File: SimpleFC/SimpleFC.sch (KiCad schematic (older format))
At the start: 0 parts

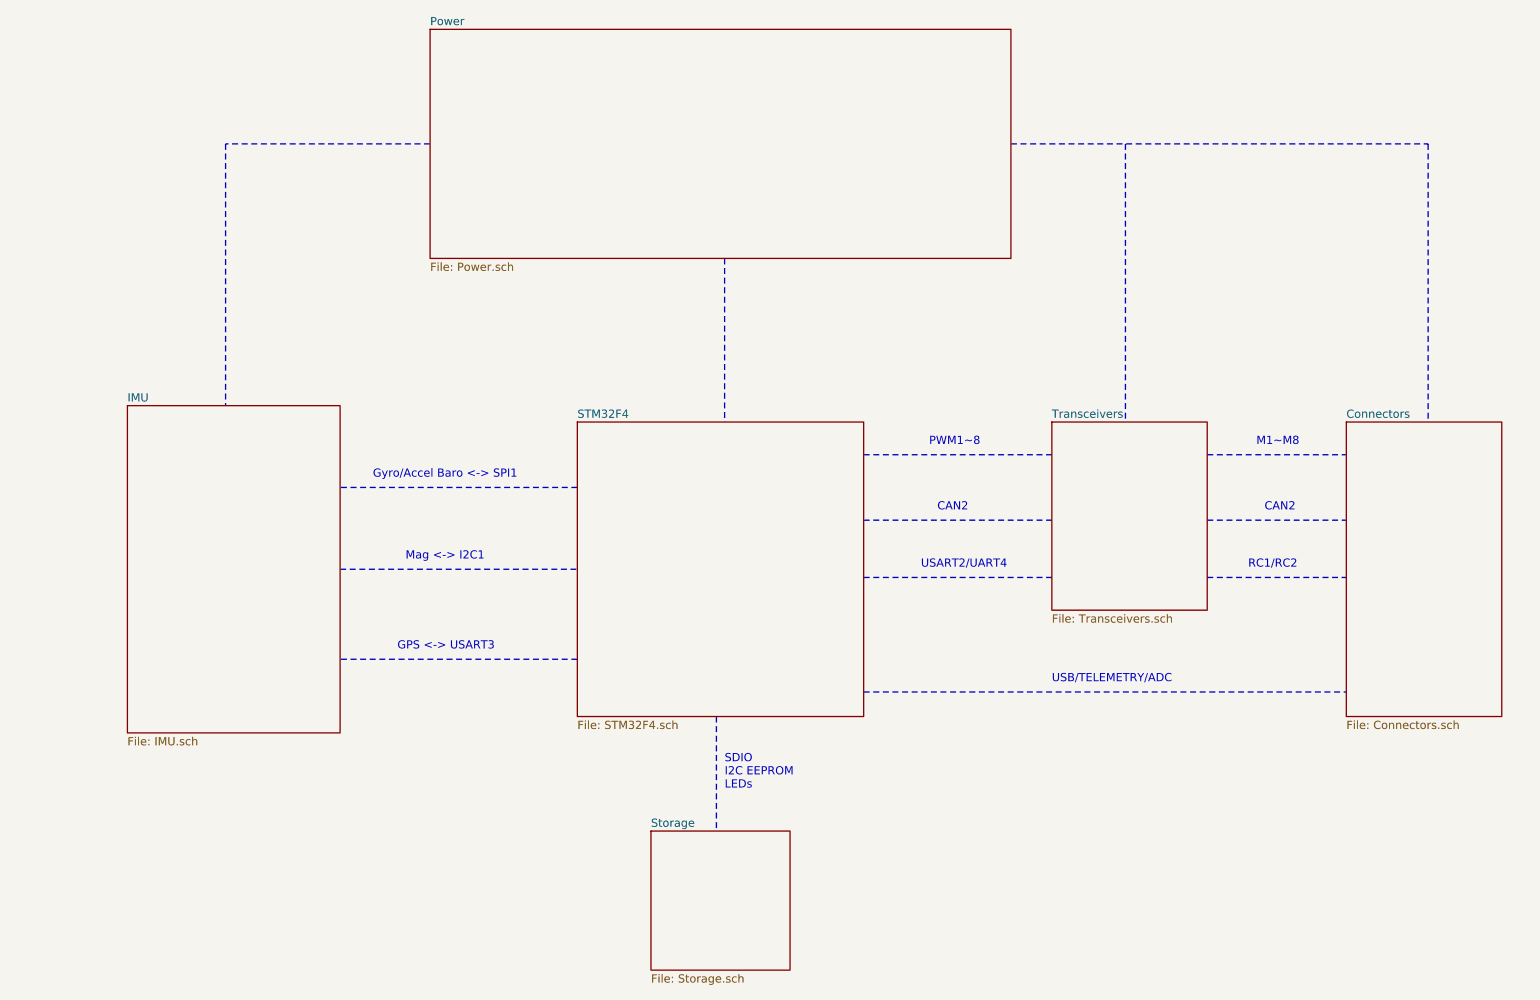
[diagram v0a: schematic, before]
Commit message: Refactor SimpleFC schematics with latest KiCAD libraries.
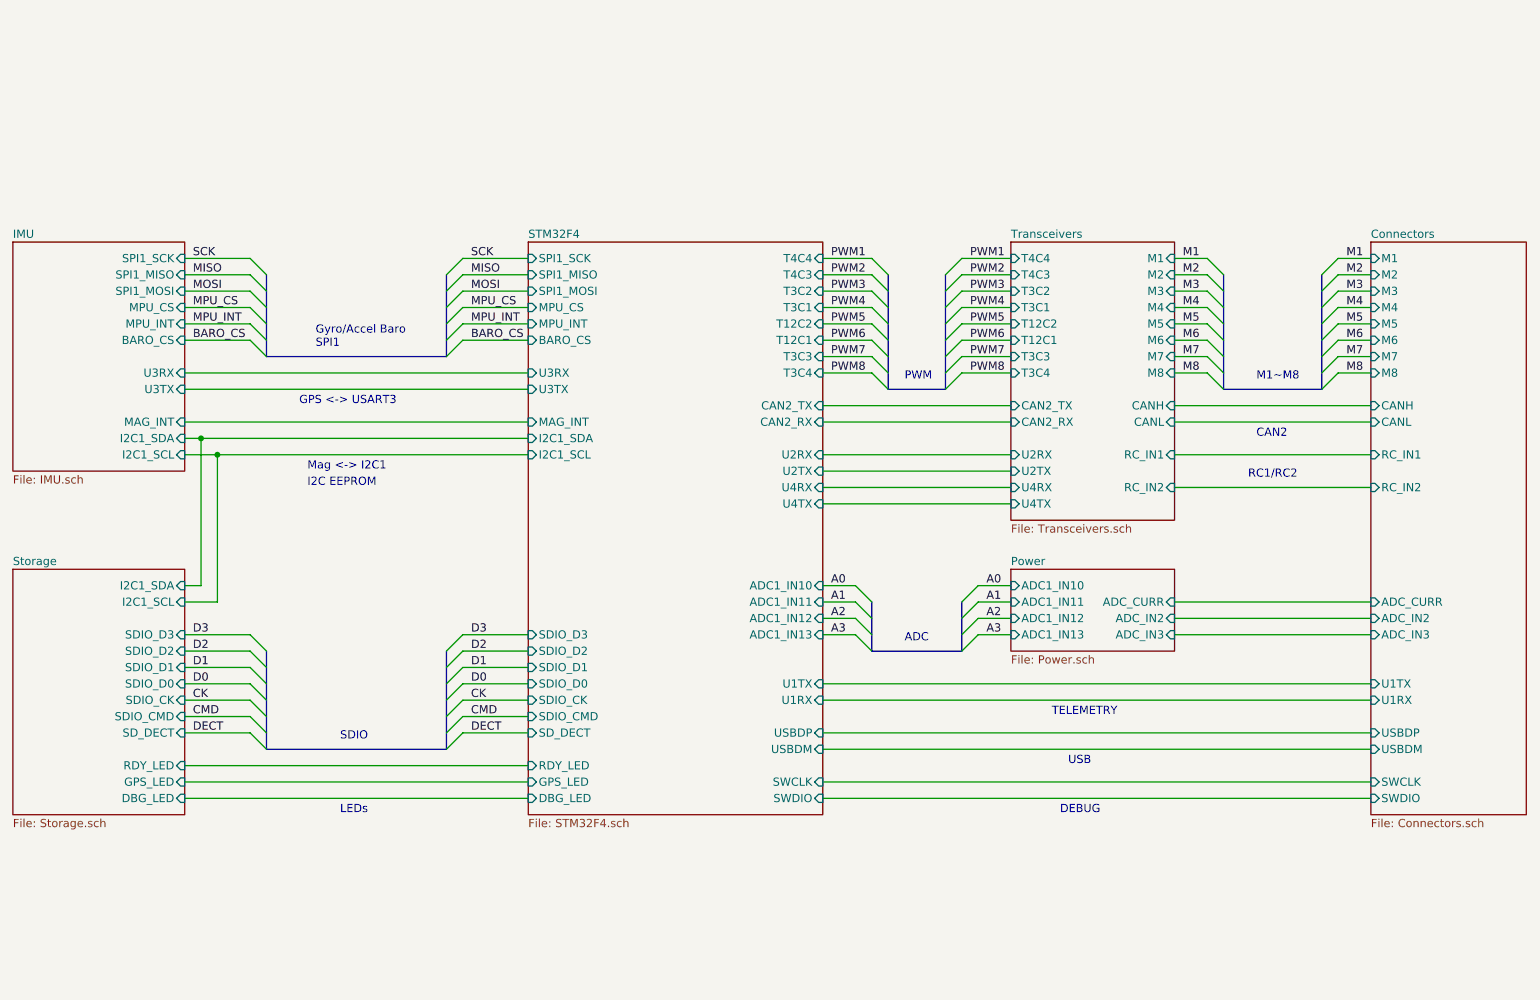
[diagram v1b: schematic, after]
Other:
- note added: "ADC"
- note added: "DEBUG"
- note added: "Gyro/Accel Baro\nSPI1"
- note added: "I2C EEPROM"
- note added: "LEDs"
- note added: "PWM"
- note added: "SDIO"
- note added: "TELEMETRY"
- note added: "USB"
- note removed: "Gyro/Accel Baro <-> SPI1"
- note removed: "PWM1~~8"
- note removed: "SDIO\nI2C EEPROM\nLEDs"
- note removed: "USART2/UART4"
- note removed: "USB/TELEMETRY/ADC"
